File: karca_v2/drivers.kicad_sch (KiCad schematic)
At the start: 15 parts, among them J10 Screw_Terminal_01x04, J11 Buzzer, J9 Screw_Terminal_01x10, Q3 IRF3708

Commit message: revisions for V2.1
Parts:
- E1, J11: footprint terminal blocks:P-2604-1102 -> custom-footprints:P-2604-1102
- J10: footprint terminal blocks:P-2604-1104 -> custom-footprints:P-2604-1104
- J9: footprint terminal blocks:P-2604-1110 -> custom-footprints:P-2604-1110

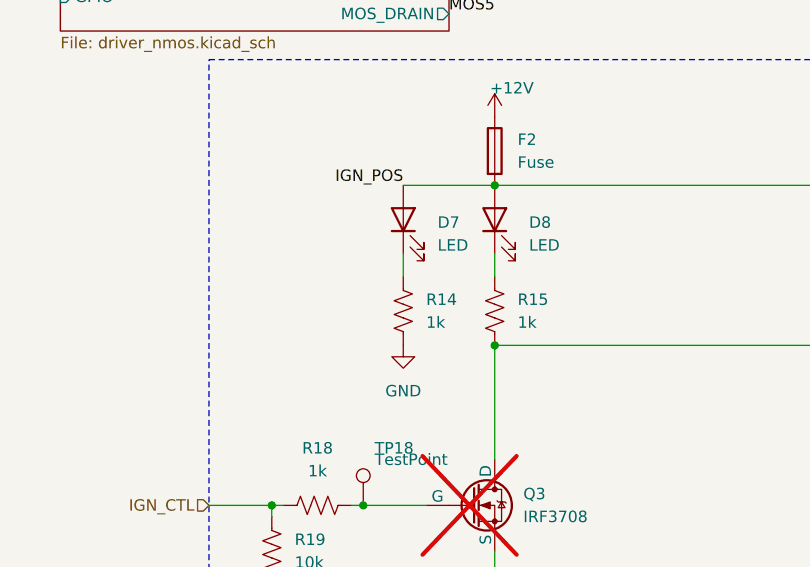
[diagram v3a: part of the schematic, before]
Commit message: finished schematic for v2.1
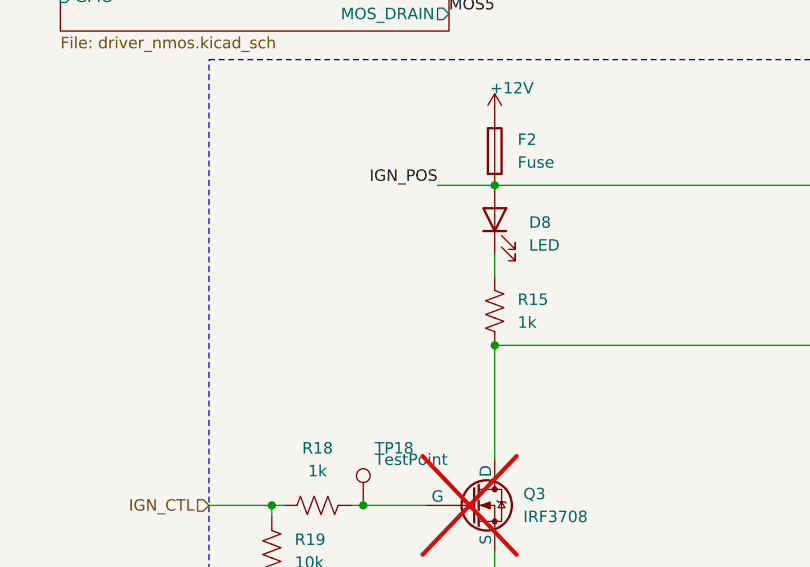
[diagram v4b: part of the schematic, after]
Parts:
- removed D7: LED, LED_SMD:LED_1206_3216Metric, symbol Device:LED
- removed R14: 1k, Resistor_SMD:R_1206_3216Metric, symbol Device:R_US
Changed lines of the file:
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@@
 	(wire
 		(pts
-			(xy 68.58 135.89) (xy 78.74 135.89)
+			(xy 72.39 135.89) (xy 78.74 135.89)
 		)
 		(stroke
@@
 		(pts
 			(xy 232.41 68.58) (xy 226.06 68.58)
-		)
-		(stroke
-			(width 0)
-			(type default)
-		)
-	)
-	(wire
-		(pts
-			(xy 68.58 143.51) (xy 68.58 146.05)
 		)
 		(stroke
@@
 	)
 	(label "IGN_POS"
-		(at 68.58 135.89 180)
+		(at 72.39 135.89 180)
 		(effects
 			(font
@@
 	)
 	(symbol
-		(lib_id "power:GND")
-		(at 68.58 153.67 0)
-		(unit 1)
-		(exclude_from_sim no)
-		(in_bom yes)
-		(on_board yes)
-		(dnp no)
-		(fields_autoplaced yes)
-		(property "Reference" "#PWR070"
-			(at 68.58 160.02 0)
-			(effects
-				(font
-					(size 1.27 1.27)
-				)
-				(hide yes)
-			)
-		)
-		(property "Value" "GND"
-			(at 68.58 158.75 0)
-			(effects
-				(font
-					(size 1.27 1.27)
-				)
-			)
-		)
-		(property "Footprint" ""
-			(at 68.58 153.67 0)
-			(effects
-				(font
-					(size 1.27 1.27)
-				)
-				(hide yes)
-			)
-		)
-		(property "Datasheet" ""
-			(at 68.58 153.67 0)
-			(effects
-				(font
-					(size 1.27 1.27)
-				)
-				(hide yes)
-			)
-		)
-		(property "Description" ""
-			(at 68.58 153.67 0)
-			(effects
-				(font
-					(size 1.27 1.27)
-				)
-				(hide yes)
-			)
-		)
-		(pin "1"
-		)
-		(instances
-			(project "karca_v2"
-				(path "/29cf4797-56f2-4f57-ae95-7df639362e3c/7dac9c60-d103-4efb-8cad-8e42b4335148"
-					(reference "#PWR070")
-					(unit 1)
-				)
-			)
-		)
-	)
-	(symbol
 		(lib_id "power:+12V")
 		(at 78.74 128.27 0)
@@
 				(path "/29cf4797-56f2-4f57-ae95-7df639362e3c/7dac9c60-d103-4efb-8cad-8e42b4335148"
 					(reference "#PWR067")
-					(unit 1)
-				)
-			)
-		)
-	)
-	(symbol
-		(lib_id "Device:LED")
-		(at 68.58 139.7 90)
-		(unit 1)
-		(exclude_from_sim no)
-		(in_bom yes)
-		(on_board yes)
-		(dnp no)
-		(fields_autoplaced yes)
-		(property "Reference" "D7"
-			(at 72.39 140.0175 90)
-			(effects
-				(font
-					(size 1.27 1.27)
-				)
-				(justify right)
-			)
-		)
-		(property "Value" "LED"
-			(at 72.39 142.5575 90)
-			(effects
-				(font
-					(size 1.27 1.27)
-				)
-				(justify right)
-			)
-		)
-		(property "Footprint" "LED_SMD:LED_1206_3216Metric"
-			(at 68.58 139.7 0)
-			(effects
-				(font
-					(size 1.27 1.27)
-				)
-				(hide yes)
-			)
-		)
-		(property "Datasheet" "~"
-			(at 68.58 139.7 0)
-			(effects
-				(font
-					(size 1.27 1.27)
-				)
-				(hide yes)
-			)
-		)
-		(property "Description" ""
-			(at 68.58 139.7 0)
-			(effects
-				(font
-					(size 1.27 1.27)
-				)
-				(hide yes)
-			)
-		)
-		(property "LCSC" "C125084"
-			(at 68.58 139.7 90)
-			(effects
-				(font
-					(size 1.27 1.27)
-				)
-				(hide yes)
-			)
-		)
-		(pin "1"
-		)
-		(pin "2"
-		)
-		(instances
-			(project "karca_v2"
-				(path "/29cf4797-56f2-4f57-ae95-7df639362e3c/7dac9c60-d103-4efb-8cad-8e42b4335148"
-					(reference "D7")
 					(unit 1)
 				)
@@
 					(unit 1)
 				)
-			)
-		)
-	)
-	(symbol
-		(lib_id "Device:R_US")
-		(at 68.58 149.86 0)
-		(unit 1)
-		(exclude_from_sim no)
-		(in_bom yes)
-		(on_board yes)
-		(dnp no)
-		(fields_autoplaced yes)
-		(property "Reference" "R14"
-			(at 71.12 148.59 0)
-			(effects
-				(font
-					(size 1.27 1.27)
-				)
-				(justify left)
-			)
-		)
-		(property "Value" "1k"
-			(at 71.12 151.13 0)
-			(effects
-				(font
-					(size 1.27 1.27)
-				)
-				(justify left)
-			)
-		)
-		(property "Footprint" "Resistor_SMD:R_1206_3216Metric"
-			(at 69.596 150.114 90)
-			(effects
-				(font
-					(size 1.27 1.27)
-				)
-				(hide yes)
-			)
-		)
-		(property "Datasheet" "~"
-			(at 68.58 149.86 0)
-			(effects
-				(font
-					(size 1.27 1.27)
-				)
-				(hide yes)
-			)
-		)
-		(property "Description" ""
-			(at 68.58 149.86 0)
-			(effects
-				(font
-					(size 1.27 1.27)
-				)
-				(hide yes)
-			)
-		)
-		(pin "1"
-		)
-		(pin "2"
-		)
-		(instances
-			(project "karca_v2"
-				(path "/29cf4797-56f2-4f57-ae95-7df639362e3c/7dac9c60-d103-4efb-8cad-8e42b4335148"
-					(reference "R14")
-					(unit 1)
-				)

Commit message: swapped adcs
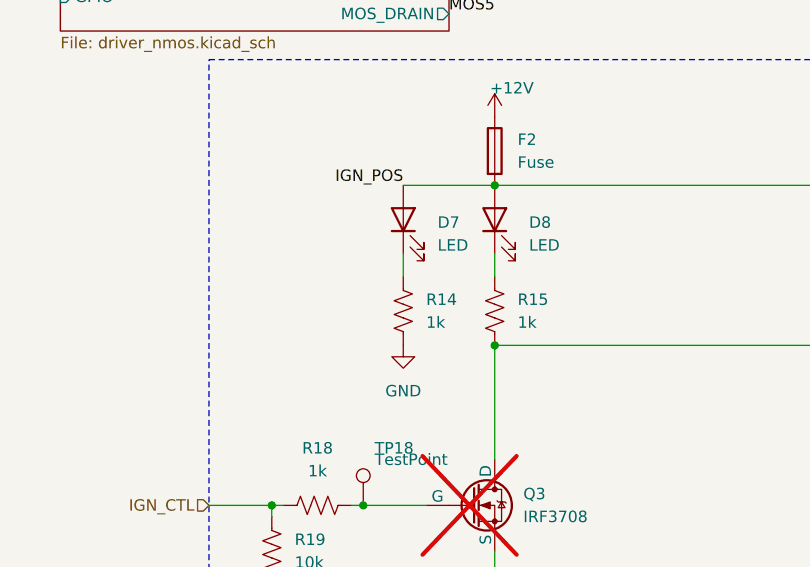
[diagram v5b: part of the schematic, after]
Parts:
- added D7: LED, LED_SMD:LED_1206_3216Metric, symbol Device:LED
- added R14: 1k, Resistor_SMD:R_1206_3216Metric, symbol Device:R_US
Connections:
- net GND: now also R14.2
- net IGN_POS: now also D7.2 (A)
- new net: D7.1 (K), R14.1
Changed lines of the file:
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@@
 	(title_block
 		(title "kARCA 2.0 Engine Control System")
-		(date "2026-03-23")
-		(rev "1.2")
+		(date "2024-12-16")
+		(rev "1.1")
 		(company "Rice Eclipse")
 		(comment 1 "Designed by Deepak Narayan")
@@
 	(wire
 		(pts
-			(xy 72.39 135.89) (xy 78.74 135.89)
+			(xy 68.58 135.89) (xy 78.74 135.89)
 		)
 		(stroke
@@
 		(pts
 			(xy 232.41 68.58) (xy 226.06 68.58)
+		)
+		(stroke
+			(width 0)
+			(type default)
+		)
+	)
+	(wire
+		(pts
+			(xy 68.58 143.51) (xy 68.58 146.05)
 		)
 		(stroke
@@
 	)
 	(label "IGN_POS"
-		(at 72.39 135.89 180)
+		(at 68.58 135.89 180)
 		(effects
 			(font
@@
 	)
 	(symbol
+		(lib_id "power:GND")
+		(at 68.58 153.67 0)
+		(unit 1)
+		(exclude_from_sim no)
+		(in_bom yes)
+		(on_board yes)
+		(dnp no)
+		(fields_autoplaced yes)
+		(property "Reference" "#PWR070"
+			(at 68.58 160.02 0)
+			(effects
+				(font
+					(size 1.27 1.27)
+				)
+				(hide yes)
+			)
+		)
+		(property "Value" "GND"
+			(at 68.58 158.75 0)
+			(effects
+				(font
+					(size 1.27 1.27)
+				)
+			)
+		)
+		(property "Footprint" ""
+			(at 68.58 153.67 0)
+			(effects
+				(font
+					(size 1.27 1.27)
+				)
+				(hide yes)
+			)
+		)
+		(property "Datasheet" ""
+			(at 68.58 153.67 0)
+			(effects
+				(font
+					(size 1.27 1.27)
+				)
+				(hide yes)
+			)
+		)
+		(property "Description" ""
+			(at 68.58 153.67 0)
+			(effects
+				(font
+					(size 1.27 1.27)
+				)
+				(hide yes)
+			)
+		)
+		(pin "1"
+		)
+		(instances
+			(project "karca_v2"
+				(path "/29cf4797-56f2-4f57-ae95-7df639362e3c/7dac9c60-d103-4efb-8cad-8e42b4335148"
+					(reference "#PWR070")
+					(unit 1)
+				)
+			)
+		)
+	)
+	(symbol
 		(lib_id "power:+12V")
 		(at 78.74 128.27 0)
@@
 				(path "/29cf4797-56f2-4f57-ae95-7df639362e3c/7dac9c60-d103-4efb-8cad-8e42b4335148"
 					(reference "#PWR067")
+					(unit 1)
+				)
+			)
+		)
+	)
+	(symbol
+		(lib_id "Device:LED")
+		(at 68.58 139.7 90)
+		(unit 1)
+		(exclude_from_sim no)
+		(in_bom yes)
+		(on_board yes)
+		(dnp no)
+		(fields_autoplaced yes)
+		(property "Reference" "D7"
+			(at 72.39 140.0175 90)
+			(effects
+				(font
+					(size 1.27 1.27)
+				)
+				(justify right)
+			)
+		)
+		(property "Value" "LED"
+			(at 72.39 142.5575 90)
+			(effects
+				(font
+					(size 1.27 1.27)
+				)
+				(justify right)
+			)
+		)
+		(property "Footprint" "LED_SMD:LED_1206_3216Metric"
+			(at 68.58 139.7 0)
+			(effects
+				(font
+					(size 1.27 1.27)
+				)
+				(hide yes)
+			)
+		)
+		(property "Datasheet" "~"
+			(at 68.58 139.7 0)
+			(effects
+				(font
+					(size 1.27 1.27)
+				)
+				(hide yes)
+			)
+		)
+		(property "Description" ""
+			(at 68.58 139.7 0)
+			(effects
+				(font
+					(size 1.27 1.27)
+				)
+				(hide yes)
+			)
+		)
+		(property "LCSC" "C125084"
+			(at 68.58 139.7 90)
+			(effects
+				(font
+					(size 1.27 1.27)
+				)
+				(hide yes)
+			)
+		)
+		(pin "1"
+		)
+		(pin "2"
+		)
+		(instances
+			(project "karca_v2"
+				(path "/29cf4797-56f2-4f57-ae95-7df639362e3c/7dac9c60-d103-4efb-8cad-8e42b4335148"
+					(reference "D7")
 					(unit 1)
 				)
@@
 					(unit 1)
 				)
+			)
+		)
+	)
+	(symbol
+		(lib_id "Device:R_US")
+		(at 68.58 149.86 0)
+		(unit 1)
+		(exclude_from_sim no)
+		(in_bom yes)
+		(on_board yes)
+		(dnp no)
+		(fields_autoplaced yes)
+		(property "Reference" "R14"
+			(at 71.12 148.59 0)
+			(effects
+				(font
+					(size 1.27 1.27)
+				)
+				(justify left)
+			)
+		)
+		(property "Value" "1k"
+			(at 71.12 151.13 0)
+			(effects
+				(font
+					(size 1.27 1.27)
+				)
+				(justify left)
+			)
+		)
+		(property "Footprint" "Resistor_SMD:R_1206_3216Metric"
+			(at 69.596 150.114 90)
+			(effects
+				(font
+					(size 1.27 1.27)
+				)
+				(hide yes)
+			)
+		)
+		(property "Datasheet" "~"
+			(at 68.58 149.86 0)
+			(effects
+				(font
+					(size 1.27 1.27)
+				)
+				(hide yes)
+			)
+		)
+		(property "Description" ""
+			(at 68.58 149.86 0)
+			(effects
+				(font
+					(size 1.27 1.27)
+				)
+				(hide yes)
+			)
+		)
+		(pin "1"
+		)
+		(pin "2"
+		)
+		(instances
+			(project "karca_v2"
+				(path "/29cf4797-56f2-4f57-ae95-7df639362e3c/7dac9c60-d103-4efb-8cad-8e42b4335148"
+					(reference "R14")
+					(unit 1)
+				)

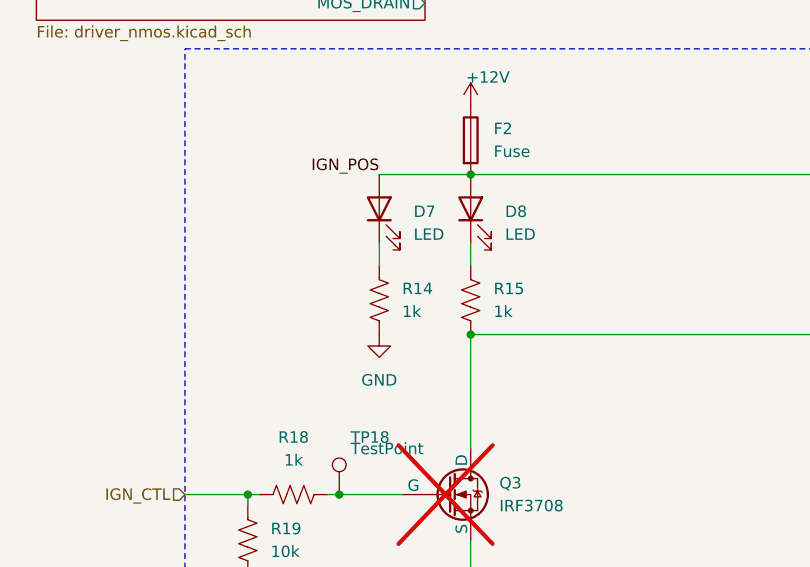
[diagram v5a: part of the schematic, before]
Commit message: Swapped IRF3708 FETs for AO3400 for more compact package
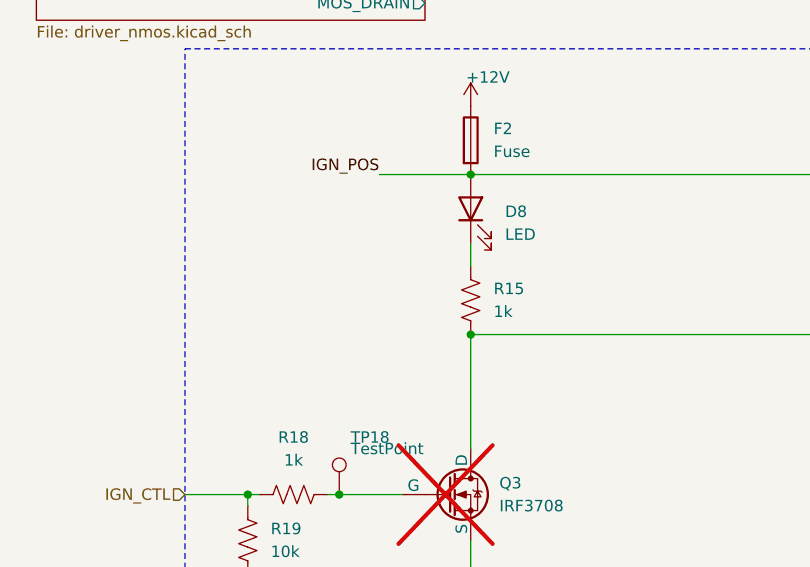
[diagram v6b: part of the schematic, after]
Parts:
- removed D7: LED, LED_SMD:LED_1206_3216Metric, symbol Device:LED
- removed R14: 1k, Resistor_SMD:R_1206_3216Metric, symbol Device:R_US
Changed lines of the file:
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@@
-	(wire
-		(pts
-			(xy 68.58 143.51) (xy 68.58 146.05)
-		)
-		(stroke
-			(width 0)
-			(type default)
-		)
-	)
 	(wire
 		(pts
@@
 	)
 	(symbol
-		(lib_id "power:GND")
-		(at 68.58 153.67 0)
-		(unit 1)
-		(exclude_from_sim no)
-		(in_bom yes)
-		(on_board yes)
-		(dnp no)
-		(fields_autoplaced yes)
-		(property "Reference" "#PWR070"
-			(at 68.58 160.02 0)
-			(effects
-				(font
-					(size 1.27 1.27)
-				)
-				(hide yes)
-			)
-		)
-		(property "Value" "GND"
-			(at 68.58 158.75 0)
-			(effects
-				(font
-					(size 1.27 1.27)
-				)
-			)
-		)
-		(property "Footprint" ""
-			(at 68.58 153.67 0)
-			(effects
-				(font
-					(size 1.27 1.27)
-				)
-				(hide yes)
-			)
-		)
-		(property "Datasheet" ""
-			(at 68.58 153.67 0)
-			(effects
-				(font
-					(size 1.27 1.27)
-				)
-				(hide yes)
-			)
-		)
-		(property "Description" ""
-			(at 68.58 153.67 0)
-			(effects
-				(font
-					(size 1.27 1.27)
-				)
-				(hide yes)
-			)
-		)
-		(pin "1"
-		)
-		(instances
-			(project "karca_v2"
-				(path "/29cf4797-56f2-4f57-ae95-7df639362e3c/7dac9c60-d103-4efb-8cad-8e42b4335148"
-					(reference "#PWR070")
-					(unit 1)
-				)
-			)
-		)
-	)
-	(symbol
 		(lib_id "power:+12V")
 		(at 78.74 128.27 0)
@@
 				(path "/29cf4797-56f2-4f57-ae95-7df639362e3c/7dac9c60-d103-4efb-8cad-8e42b4335148"
 					(reference "#PWR067")
-					(unit 1)
-				)
-			)
-		)
-	)
-	(symbol
-		(lib_id "Device:LED")
-		(at 68.58 139.7 90)
-		(unit 1)
-		(exclude_from_sim no)
-		(in_bom yes)
-		(on_board yes)
-		(dnp no)
-		(fields_autoplaced yes)
-		(property "Reference" "D7"
-			(at 72.39 140.0175 90)
-			(effects
-				(font
-					(size 1.27 1.27)
-				)
-				(justify right)
-			)
-		)
-		(property "Value" "LED"
-			(at 72.39 142.5575 90)
-			(effects
-				(font
-					(size 1.27 1.27)
-				)
-				(justify right)
-			)
-		)
-		(property "Footprint" "LED_SMD:LED_1206_3216Metric"
-			(at 68.58 139.7 0)
-			(effects
-				(font
-					(size 1.27 1.27)
-				)
-				(hide yes)
-			)
-		)
-		(property "Datasheet" "~"
-			(at 68.58 139.7 0)
-			(effects
-				(font
-					(size 1.27 1.27)
-				)
-				(hide yes)
-			)
-		)
-		(property "Description" ""
-			(at 68.58 139.7 0)
-			(effects
-				(font
-					(size 1.27 1.27)
-				)
-				(hide yes)
-			)
-		)
-		(property "LCSC" "C125084"
-			(at 68.58 139.7 90)
-			(effects
-				(font
-					(size 1.27 1.27)
-				)
-				(hide yes)
-			)
-		)
-		(pin "1"
-		)
-		(pin "2"
-		)
-		(instances
-			(project "karca_v2"
-				(path "/29cf4797-56f2-4f57-ae95-7df639362e3c/7dac9c60-d103-4efb-8cad-8e42b4335148"
-					(reference "D7")
 					(unit 1)
 				)
@@
 					(unit 1)
 				)
-			)
-		)
-	)
-	(symbol
-		(lib_id "Device:R_US")
-		(at 68.58 149.86 0)
-		(unit 1)
-		(exclude_from_sim no)
-		(in_bom yes)
-		(on_board yes)
-		(dnp no)
-		(fields_autoplaced yes)
-		(property "Reference" "R14"
-			(at 71.12 148.59 0)
-			(effects
-				(font
-					(size 1.27 1.27)
-				)
-				(justify left)
-			)
-		)
-		(property "Value" "1k"
-			(at 71.12 151.13 0)
-			(effects
-				(font
-					(size 1.27 1.27)
-				)
-				(justify left)
-			)
-		)
-		(property "Footprint" "Resistor_SMD:R_1206_3216Metric"
-			(at 69.596 150.114 90)
-			(effects
-				(font
-					(size 1.27 1.27)
-				)
-				(hide yes)
-			)
-		)
-		(property "Datasheet" "~"
-			(at 68.58 149.86 0)
-			(effects
-				(font
-					(size 1.27 1.27)
-				)
-				(hide yes)
-			)
-		)
-		(property "Description" ""
-			(at 68.58 149.86 0)
-			(effects
-				(font
-					(size 1.27 1.27)
-				)
-				(hide yes)
-			)
-		)
-		(pin "1"
-		)
-		(pin "2"
-		)
-		(instances
-			(project "karca_v2"
-				(path "/29cf4797-56f2-4f57-ae95-7df639362e3c/7dac9c60-d103-4efb-8cad-8e42b4335148"
-					(reference "R14")
-					(unit 1)
-				)

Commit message: All tests passed. Going to run DFM next
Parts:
- removed Q3: IRF3708, Package_TO_SOT_THT:TO-220-3_Vertical, symbol Simulation_SPICE:NMOS
- added Q4: AO3400A, Package_TO_SOT_SMD:SOT-23, symbol Transistor_FET:AO3400A
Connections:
- net GND: now also Q4.2 (S)
- net IGN_NEG: now also Q4.3 (D)
- net at R18.2, TP18.1: now also Q4.1 (G)
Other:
- note added: "ignition"
- note removed: "Load Cell circuit"
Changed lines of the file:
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@@
 	(title_block
 		(title "kARCA 2.0 Engine Control System")
-		(date "2024-12-16")
+		(date "2026-03-25")
 		(rev "1.1")
 		(company "Rice Eclipse")
@@
 		)
 	)
-	(text "Load Cell circuit"
+	(text "ignition\n"
 		(exclude_from_sim no)
 		(at 236.22 125.095 0)
@@
 	)
 	(symbol
+		(lib_id "Transistor_FET:AO3400A")
+		(at 76.2 171.45 0)
+		(unit 1)
+		(exclude_from_sim no)
+		(in_bom yes)
+		(on_board yes)
+		(dnp no)
+		(fields_autoplaced yes)
+		(property "Reference" "Q4"
+			(at 82.55 170.1799 0)
+			(effects
+				(font
+					(size 1.27 1.27)
+				)
+				(justify left)
+			)
+		)
+		(property "Value" "AO3400A"
+			(at 82.55 172.7199 0)
+			(effects
+				(font
+					(size 1.27 1.27)
+				)
+				(justify left)
+			)
+		)
+		(property "Footprint" "Package_TO_SOT_SMD:SOT-23"
+			(at 81.28 173.355 0)
+			(effects
+				(font
+					(size 1.27 1.27)
+					(italic yes)
+				)
+				(justify left)
+				(hide yes)
+			)
+		)
+		(property "Datasheet" "http://www.aosmd.com/pdfs/datasheet/AO3400A.pdf"
+			(at 81.28 175.26 0)
+			(effects
+				(font
+					(size 1.27 1.27)
+				)
+				(justify left)
+				(hide yes)
+			)
+		)
+		(property "Description" "30V Vds, 5.7A Id, N-Channel MOSFET, SOT-23"
+			(at 76.2 171.45 0)
+			(effects
+				(font
+					(size 1.27 1.27)
+				)
+				(hide yes)
+			)
+		)
+		(pin "2"
+		)
+		(pin "3"
+		)
+		(pin "1"
+		)
+		(instances
+			(project "karca_v2"
+				(path "/29cf4797-56f2-4f57-ae95-7df639362e3c/7dac9c60-d103-4efb-8cad-8e42b4335148"
+					(reference "Q4")
+					(unit 1)
+				)
+			)
+		)
+	)
+	(symbol
 		(lib_id "Device:R_US")
 		(at 140.335 157.48 0)
@@
 					(unit 1)
 				)
-			)
-		)
-	)
-	(symbol
-		(lib_id "Simulation_SPICE:NMOS")
-		(at 76.2 171.45 0)
-		(unit 1)
-		(exclude_from_sim no)
-		(in_bom no)
-		(on_board yes)
-		(dnp yes)
-		(fields_autoplaced yes)
-		(property "Reference" "Q3"
-			(at 81.915 170.18 0)
-			(effects
-				(font
-					(size 1.27 1.27)
-				)
-				(justify left)
-			)
-		)
-		(property "Value" "IRF3708"
-			(at 81.915 172.72 0)
-			(effects
-				(font
-					(size 1.27 1.27)
-				)
-				(justify left)
-			)
-		)
-		(property "Footprint" "Package_TO_SOT_THT:TO-220-3_Vertical"
-			(at 81.28 168.91 0)
-			(effects
-				(font
-					(size 1.27 1.27)
-				)
-				(hide yes)
-			)
-		)
-		(property "Datasheet" "https://ngspice.sourceforge.io/docs/ngspice-manual.pdf"
-			(at 76.2 184.15 0)
-			(effects
-				(font
-					(size 1.27 1.27)
-				)
-				(hide yes)
-			)
-		)
-		(property "Description" ""
-			(at 76.2 171.45 0)
-			(effects
-				(font
-					(size 1.27 1.27)
-				)
-				(hide yes)
-			)
-		)
-		(property "Sim.Device" "NMOS"
-			(at 76.2 188.595 0)
-			(effects
-				(font
-					(size 1.27 1.27)
-				)
-				(hide yes)
-			)
-		)
-		(property "Sim.Type" "VDMOS"
-			(at 76.2 190.5 0)
-			(effects
-				(font
-					(size 1.27 1.27)
-				)
-				(hide yes)
-			)
-		)
-		(property "Sim.Pins" "1=D 2=G 3=S"
-			(at 76.2 186.69 0)
-			(effects
-				(font
-					(size 1.27 1.27)
-				)
-				(hide yes)
-			)
-		)
-		(pin "1"
-		)
-		(pin "3"
-		)
-		(pin "2"
-		)
-		(instances
-			(project "karca_v2"
-				(path "/29cf4797-56f2-4f57-ae95-7df639362e3c/7dac9c60-d103-4efb-8cad-8e42b4335148"
-					(reference "Q3")
-					(unit 1)
-				)
